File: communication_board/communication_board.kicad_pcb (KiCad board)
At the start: 2 copper layers, 103 x 100 mm, 44 parts, among them J1 USB_IN, J2 IMU, J3 MINI_FUSE, J4 Motors, U1 FE1.1s, U2 FT232RL, U3 FT232RL, U4 MAX485E, Y1 Crystal

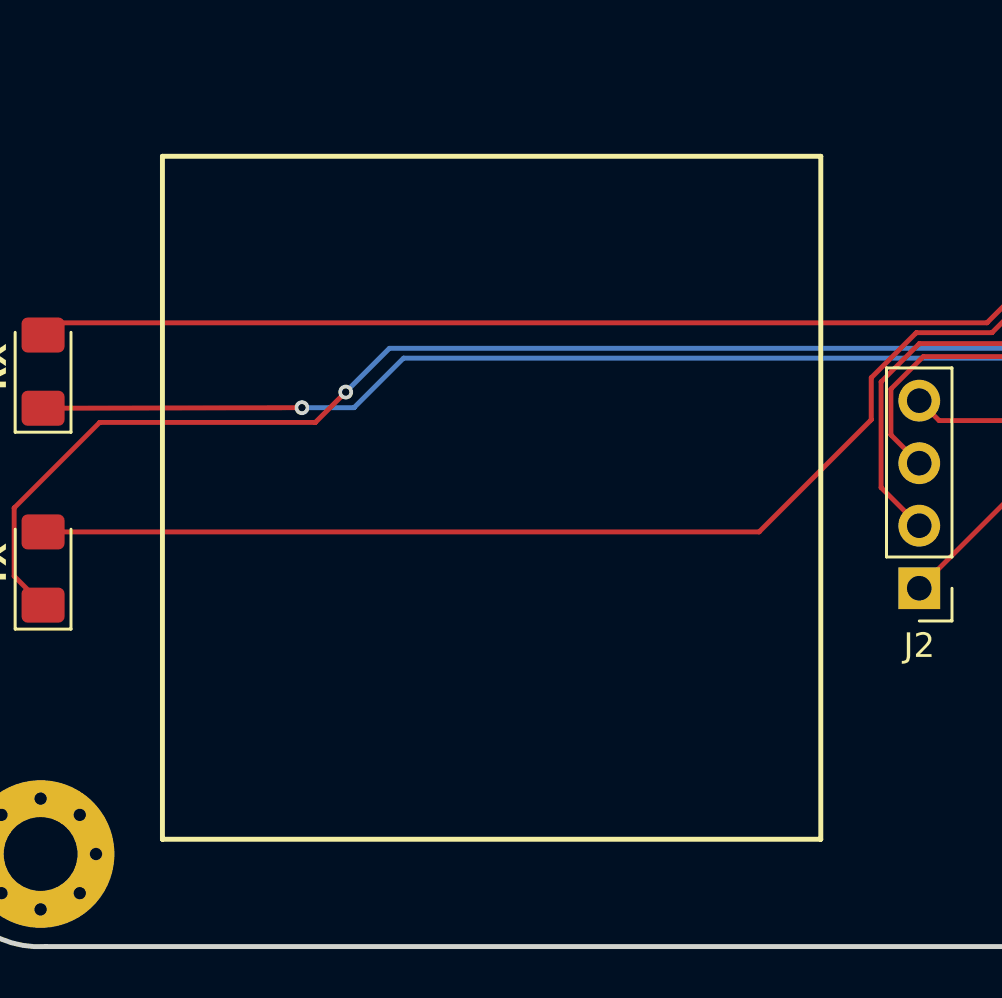
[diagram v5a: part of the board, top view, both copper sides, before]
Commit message: board with imu holes
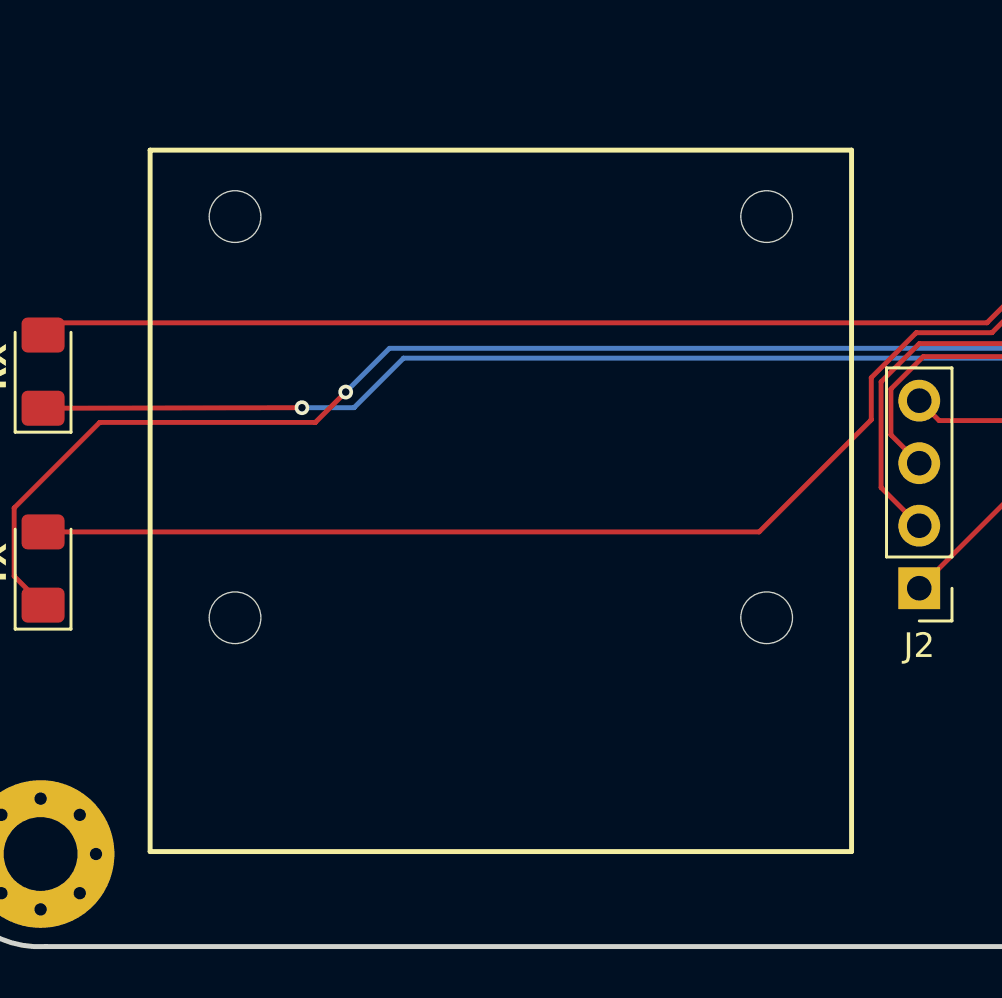
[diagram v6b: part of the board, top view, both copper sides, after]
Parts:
- added ?: , , F.Cu at (132.8, 109.5)
- added ?: , , F.Cu at (132.8, 93.2)
- added ?: , , F.Cu at (111.2, 109.5)
- added ?: , , F.Cu at (111.2, 93.2)

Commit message: Lista de materiais e plano terra
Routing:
- net Net-(D4-A): track 60.6 -> 72.7 mm
- net Net-(D5-A): track 45.5 -> 52.5 mm
- net Net-(D4-K): track 60.9 -> 63.5 mm
- net GNDREF: track 338.7 -> 339.6 mm
- added copper zone on F.Cu, net GNDREF

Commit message: pequenas mudanças
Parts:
- added G***: LOGO, Humanoid:logo_media, F.Cu at (116.2, 35.7)
- added REF**: pcb_identification, Humanoid:pcb_identification, F.Cu at (131.7, 34.9)
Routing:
- net Net-(D5-K): track 53.9 -> 52.3 mm
- net GNDREF: track 339.6 -> 340.6 mm
- net IMU_USB_D+: track 27.7 -> 28.3 mm
- net IMU_USB_D-: track 27.9 -> 28.5 mm
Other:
- board text added: "JLCJLCJLCJLC"
